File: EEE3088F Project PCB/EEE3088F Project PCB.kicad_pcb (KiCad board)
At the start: 2 copper layers, 80 x 54.9 mm, 65 parts, among them IC1 74LVC1G04SE-7, J1 JST PH 2.00mm connector, SW1 SS12D07VG5 087, U1 DRV8833PWR, U10 LM7805L-TF3-T, U11 TC4056A., U2 DRV8833PWPR, U3 INA219AxD, U4 CH224K, U6 MIC5504-1.2YM5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

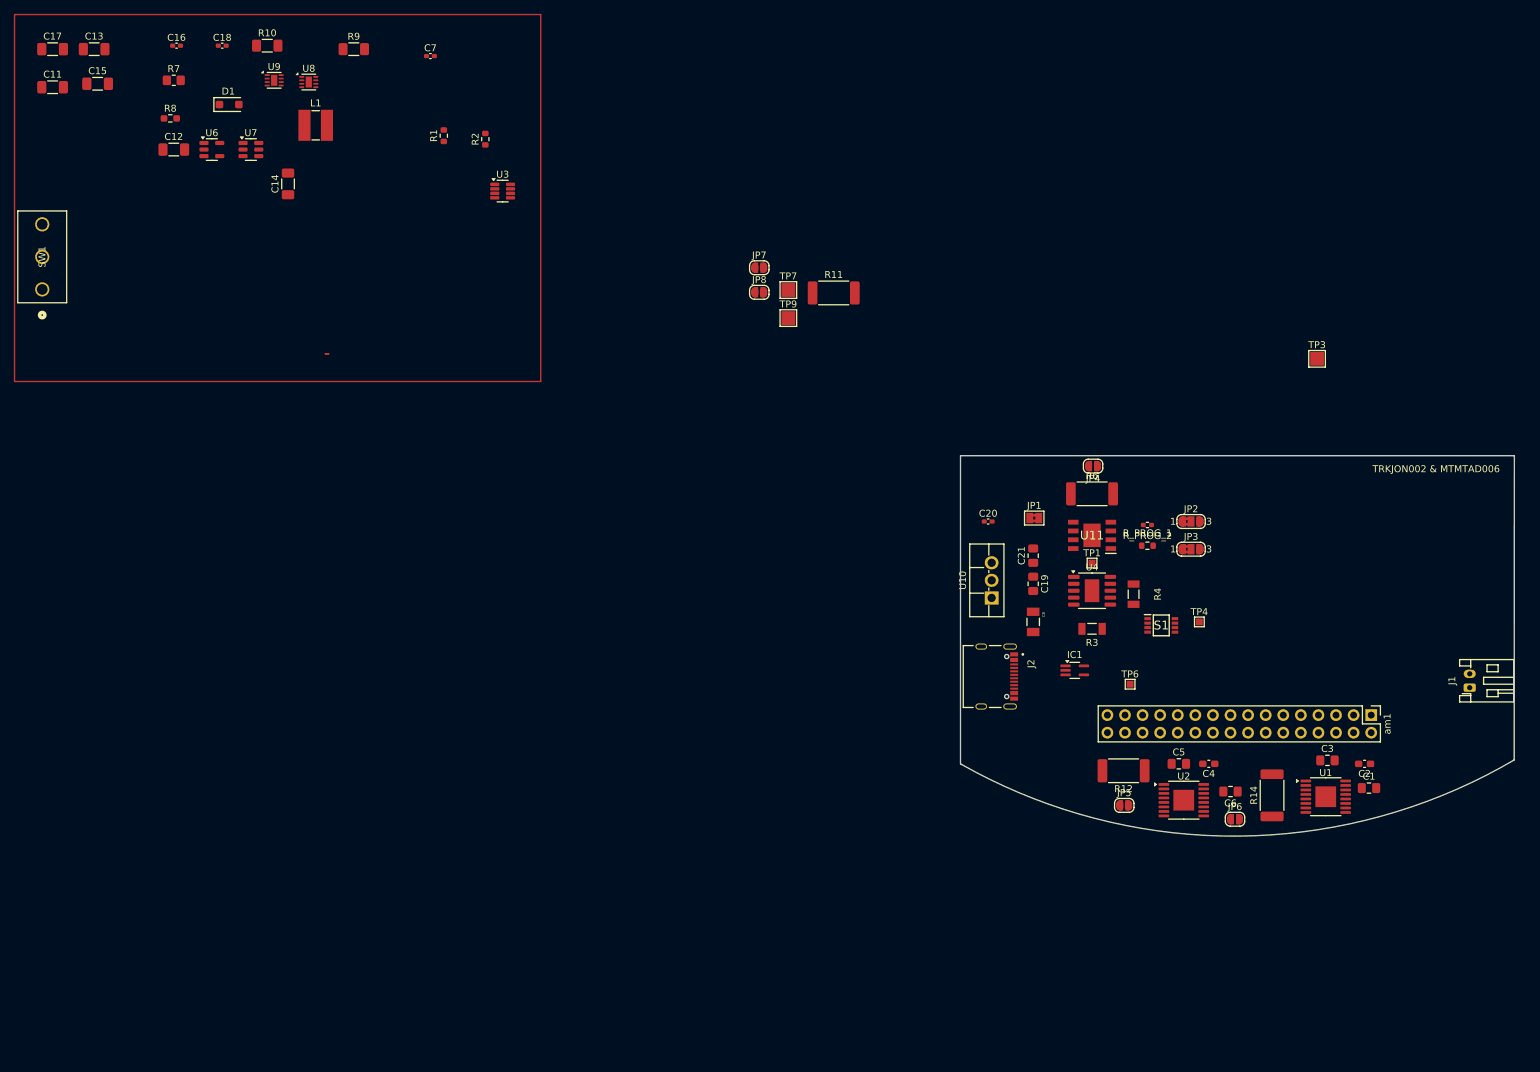
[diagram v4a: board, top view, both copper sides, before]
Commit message: confimed all tadala footprints, as well as placed all footprints on PCB board
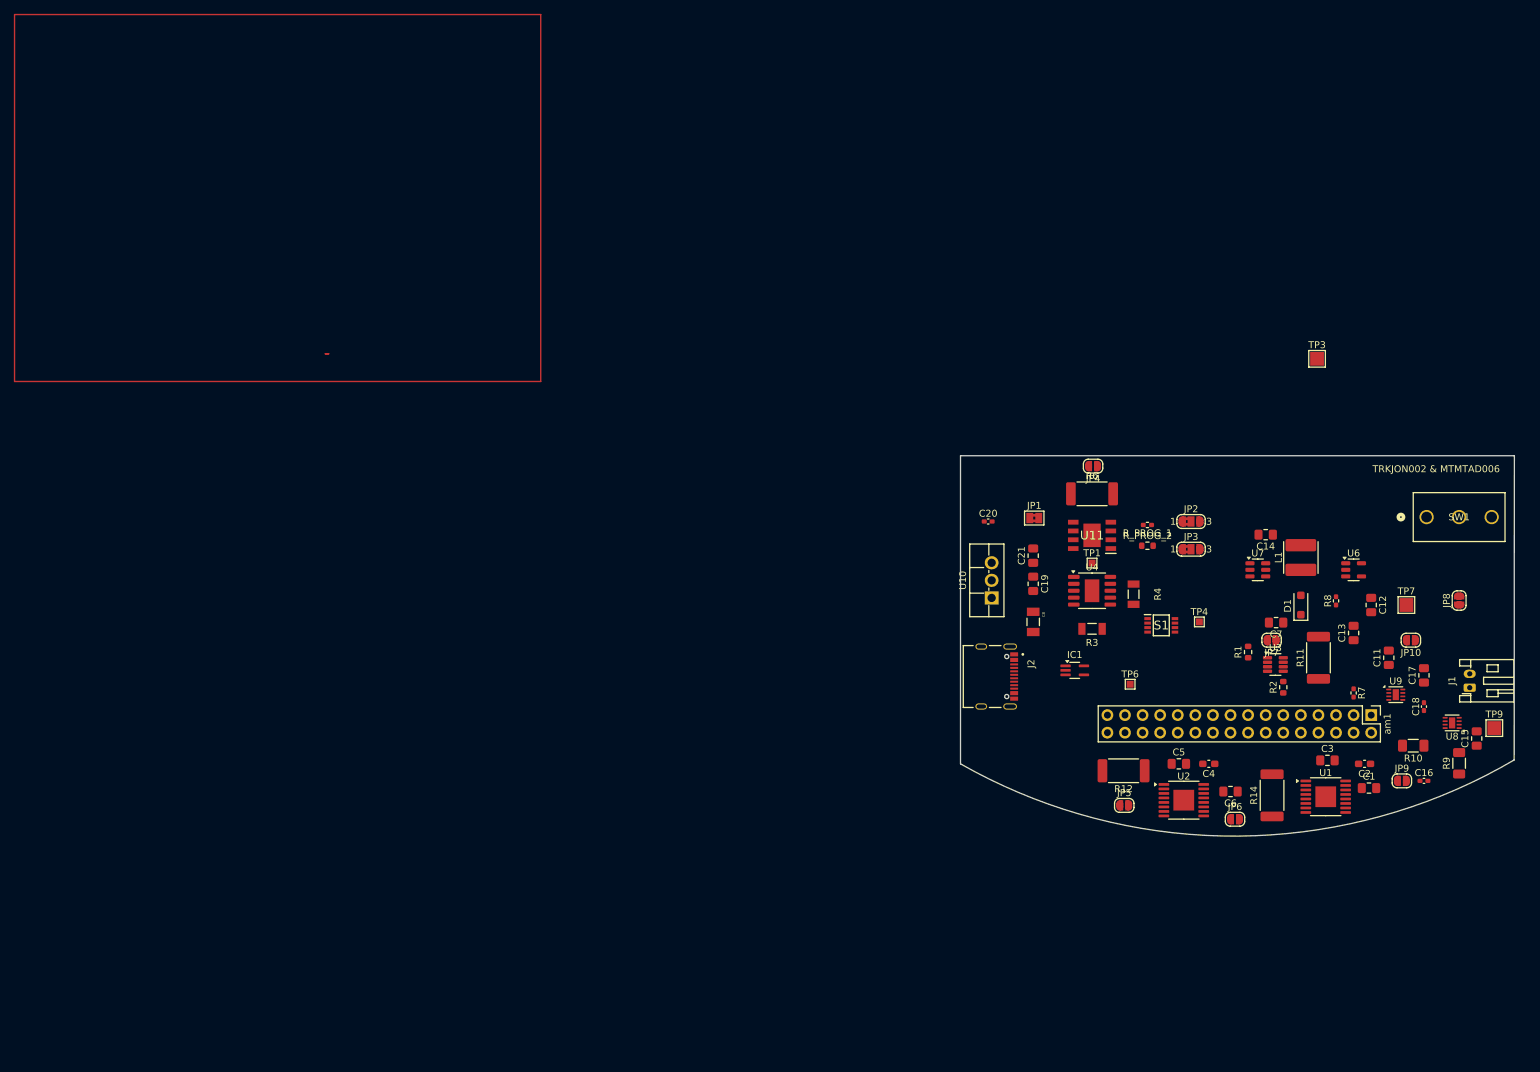
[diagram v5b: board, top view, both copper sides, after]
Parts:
- added JP10: SolderJumper_2_Open, Jumper:SolderJumper-2_P1.3mm_Open_RoundedPad1.0x1.5mm, F.Cu at (216.6, 104.1)
- added JP9: SolderJumper_2_Open, Jumper:SolderJumper-2_P1.3mm_Open_RoundedPad1.0x1.5mm, F.Cu at (215.2, 124.5)
- C11, C12, C13, C14, C15, C17: footprint Capacitor_SMD:C_1206_3216Metric_Pad1.33x1.80mm_HandSolder -> Capacitor_SMD:C_0805_2012Metric_Pad1.18x1.45mm_HandSolder
- C7: footprint Capacitor_SMD:C_0402_1005Metric_Pad0.74x0.62mm_HandSolder -> Capacitor_SMD:C_0805_2012Metric_Pad1.18x1.45mm_HandSolder
- L1: footprint Inductor_SMD:L_Ferrocore_DLG-0403 -> Inductor_SMD:L_Coilcraft_1515SQ-47N
- R7: footprint Resistor_SMD:R_0805_2012Metric_Pad1.20x1.40mm_HandSolder -> Resistor_SMD:R_0402_1005Metric_Pad0.72x0.64mm_HandSolder
- R8: footprint Resistor_SMD:R_0603_1608Metric_Pad0.98x0.95mm_HandSolder -> Resistor_SMD:R_0402_1005Metric_Pad0.72x0.64mm_HandSolder
- moved C15 220.5 mm to (226.1, 118.3), turned to 90 degrees
- moved C17 217.7 mm to (218.4, 109.2), turned to 90 degrees
- moved C11 209.8 mm to (213.4, 106.7), turned to 90 degrees
- moved C16 209.1 mm to (218.4, 124.5)
- moved SW1 202.6 mm to (218.8, 86.4), turned to 0 degrees
- moved C13 200.5 mm to (208.3, 103.1), turned to 90 degrees
- moved C18 198.1 mm to (218.4, 113.7), turned to 90 degrees
- moved R10 194.0 mm to (216.9, 119.4), turned to 180 degrees
- moved R7 192.0 mm to (208.3, 111.8), turned to -90 degrees
- moved R9 190.1 mm to (223.5, 121.9), turned to 90 degrees
- moved U8 189.3 mm to (222.5, 116.1), turned to 180 degrees
- moved C12 185.0 mm to (210.8, 99.1), turned to -90 degrees
- moved U9 184.7 mm to (214.4, 112.0)
- moved R8 182.2 mm to (205.7, 98.5), turned to 90 degrees
- moved U6 175.7 mm to (208.3, 94.0)
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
